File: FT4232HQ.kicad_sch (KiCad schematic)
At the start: 31 parts, among them IC3 USBLC6-2SC6, J4 USB_B_Micro, U15 FT4232H, U3 MCP1703T-3302E/CB, Y2 12MHz

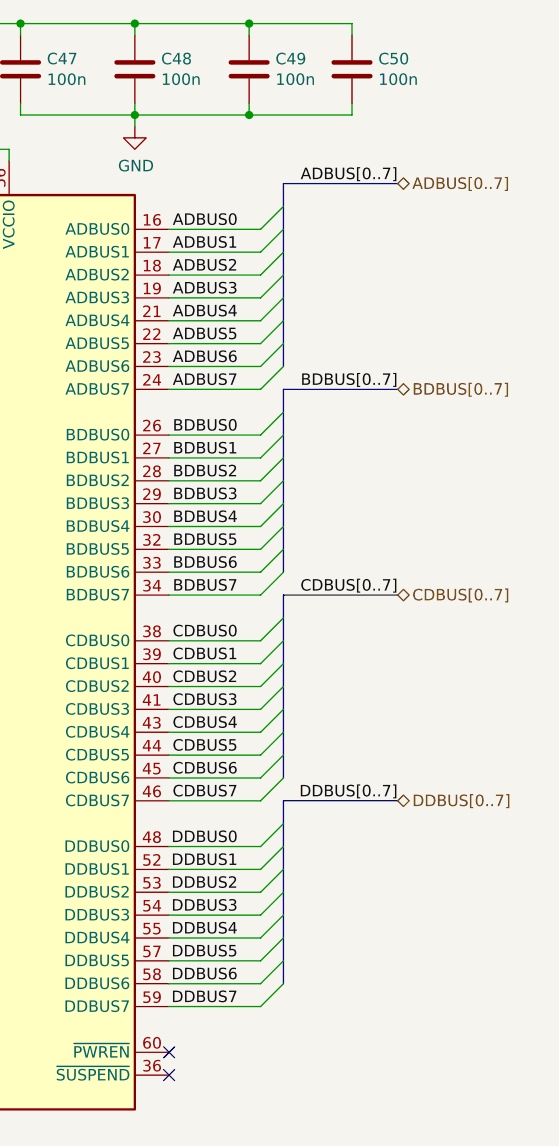
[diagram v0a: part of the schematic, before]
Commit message: minor changes for ERC
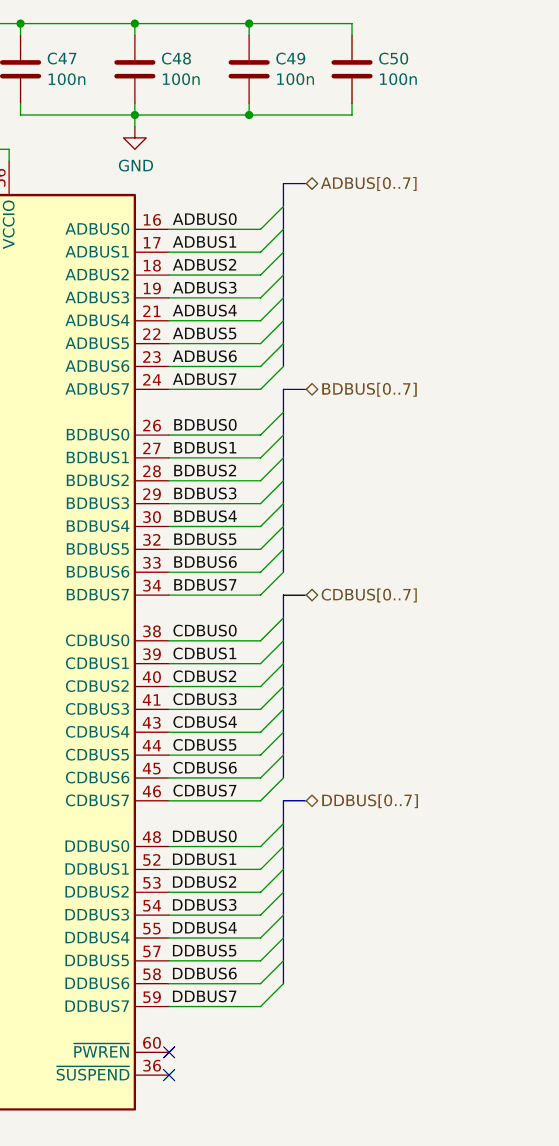
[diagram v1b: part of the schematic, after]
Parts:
- C34, C35: Unit Price 0.01 -> 0.02524194
- C36, C38, C40, C41, C42, C44, C46, C47, C48, C49, C50, C51: Unit Price 0.01 -> 0.00989262
- C37, C39: Unit Price 0.01 -> 0.0232902
- C43, C45: Unit Price 0.01 -> 0.05282334
- FB3, FB4: Unit Price 0.01 -> 0.0078741
- IC3: MPN USBLC6-2SC6 -> USBLC6-4SC6; Unit Price 0.35 -> 0.18
- J4: Unit Price 0.14 -> 0.17214714
- R59, R64: Unit Price 0.01 -> 0.0037269
- R60, R61: Unit Price 0.01 -> 0.00785034
- R62: Unit Price 0.01 -> 0.02096514
- R63: Unit Price 0.01 -> 0.03862746
- U15: Unit Price (none) -> 9.5256
- U3: Unit Price 0.40 -> 0.36599994
- Y2: Unit Price 0.20 -> 0.2218284
